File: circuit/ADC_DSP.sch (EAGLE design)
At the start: 57 parts, among them IC1 REG1117, IC3 STM32F40XRXT6, IC4 CS4272, Q1 8MHz, Q2 24.576MHz

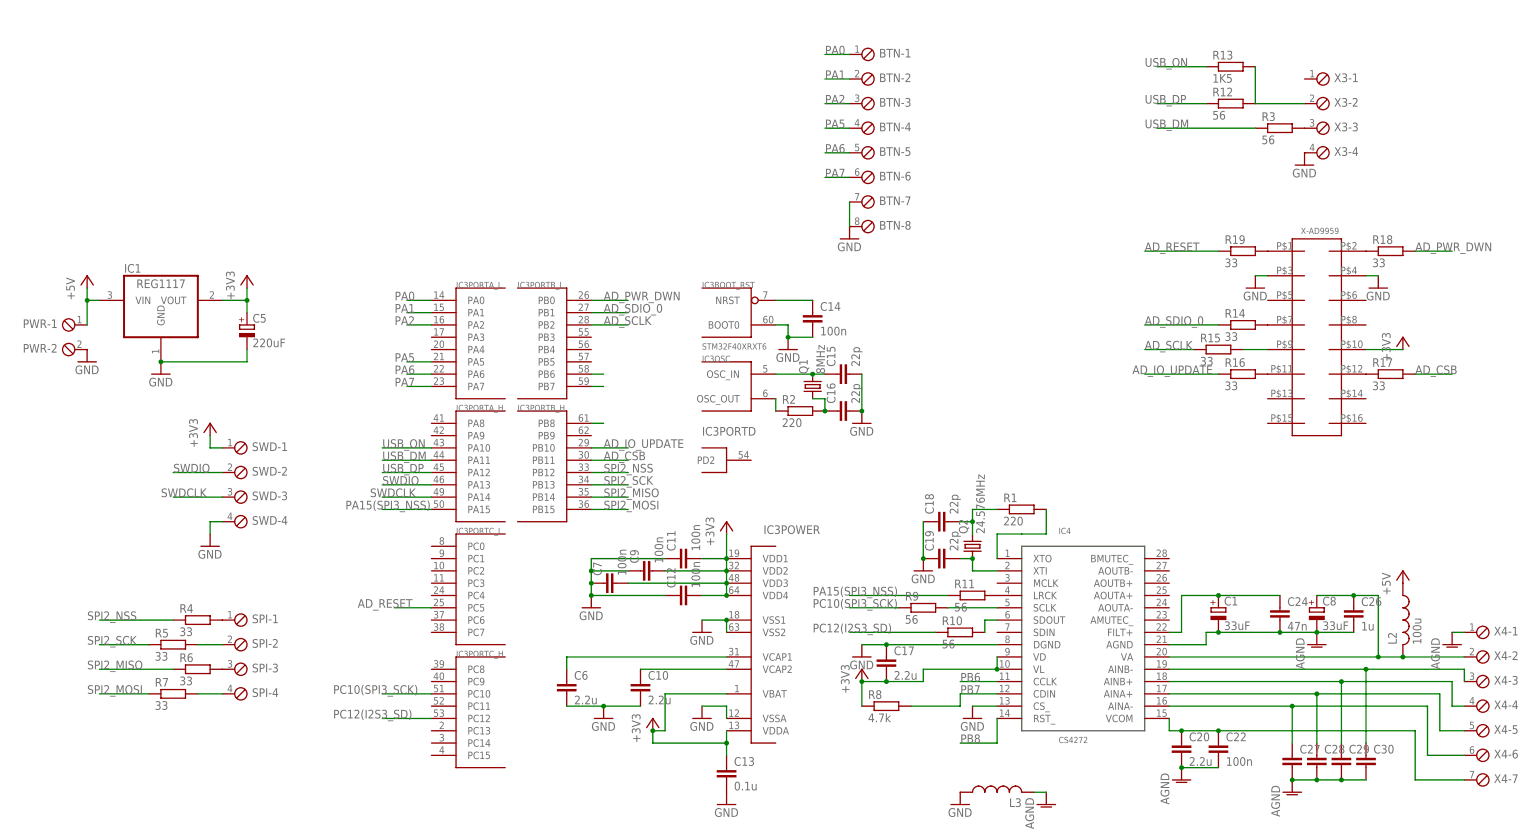
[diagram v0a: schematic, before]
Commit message: - добавили LCD разъем
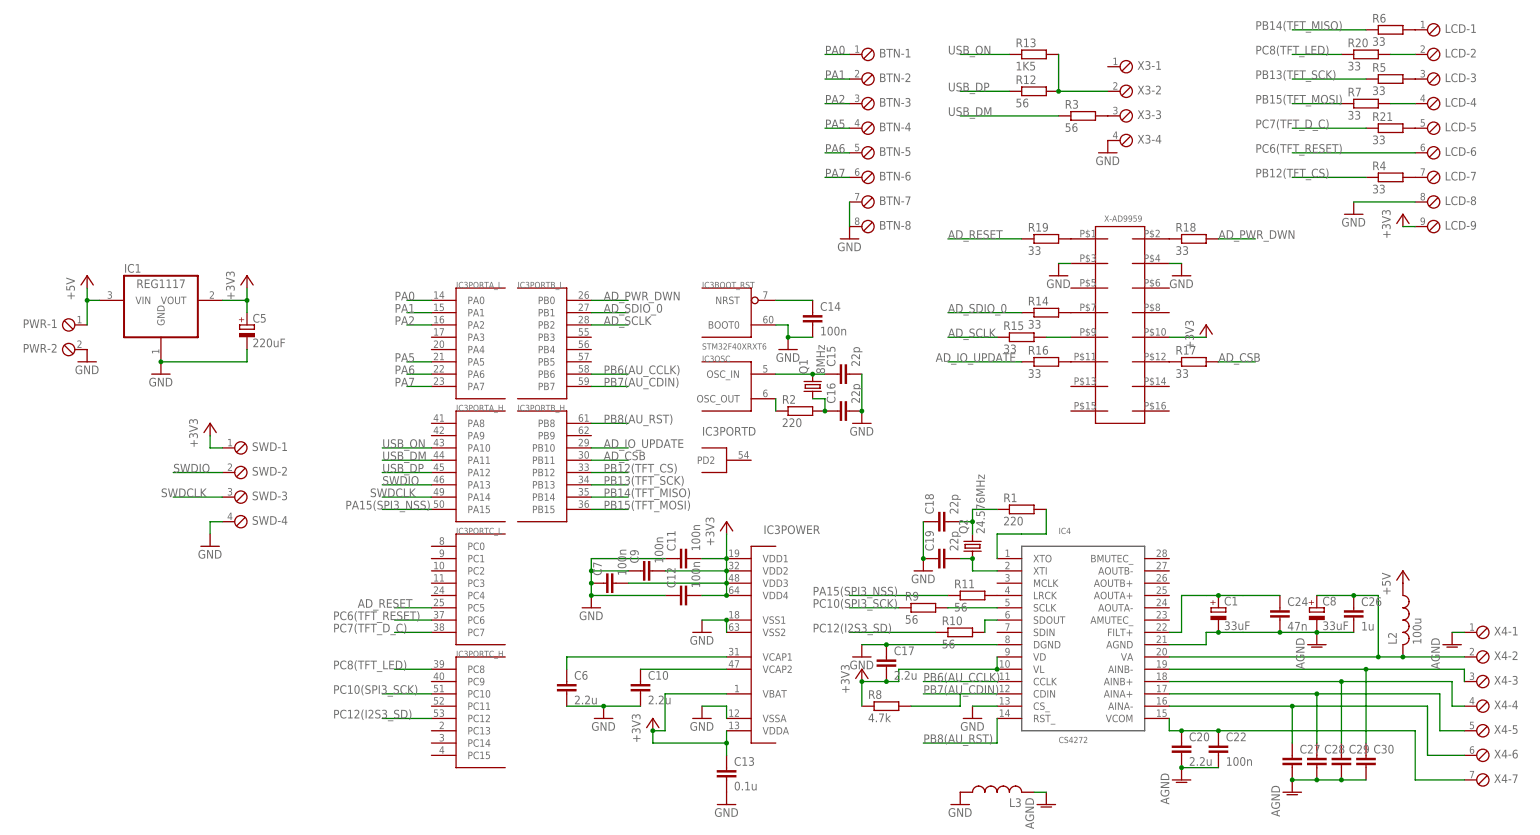
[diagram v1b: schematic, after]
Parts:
- removed SPI: (no value), con-phoenix-254:MPT4
- added LCD: (no value), con-phoenix-254:MPT9
- added R20, R21: 33, rcl:R-EU_R0603
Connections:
- net PB6 renamed PB6(AU_CCLK)
- net PB7 renamed PB7(AU_CDIN)
- net PB8 renamed PB8(AU_RST)
- net SPI2_MISO renamed PB14(TFT_MISO)
- net SPI2_MOSI renamed PB15(TFT_MOSI)
- net SPI2_NSS renamed PB12(TFT_CS)
- net SPI2_SCK renamed PB13(TFT_SCK)
- new net N$34: LCD-7.1, R4.2
- new net N$35: LCD-5.1, R21.2
- new net PC6(TFT_RESET): IC3PORTC_L.PC6, LCD-6.1
- new net PC7(TFT_D_C): IC3PORTC_L.PC7, R21.1
- new net PC8(TFT_LED): IC3PORTC_H.PC8, R20.1
- net +3V3: now also LCD-9.1
- net GND: now also LCD-8.1
- net N$20: now also LCD-1.1, R6.2; no longer R4.2, SPI-1.1
- net N$21: now also LCD-3.1; no longer SPI-2.1
- net N$22: now also LCD-2.1, R20.2; no longer R6.2, SPI-3.1
- net N$24: now also LCD-4.1; no longer SPI-4.1
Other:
- moved on the sheet: R12, R13, R14, R15, R16, R17, R18, R19, R3, R4, R5, R6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

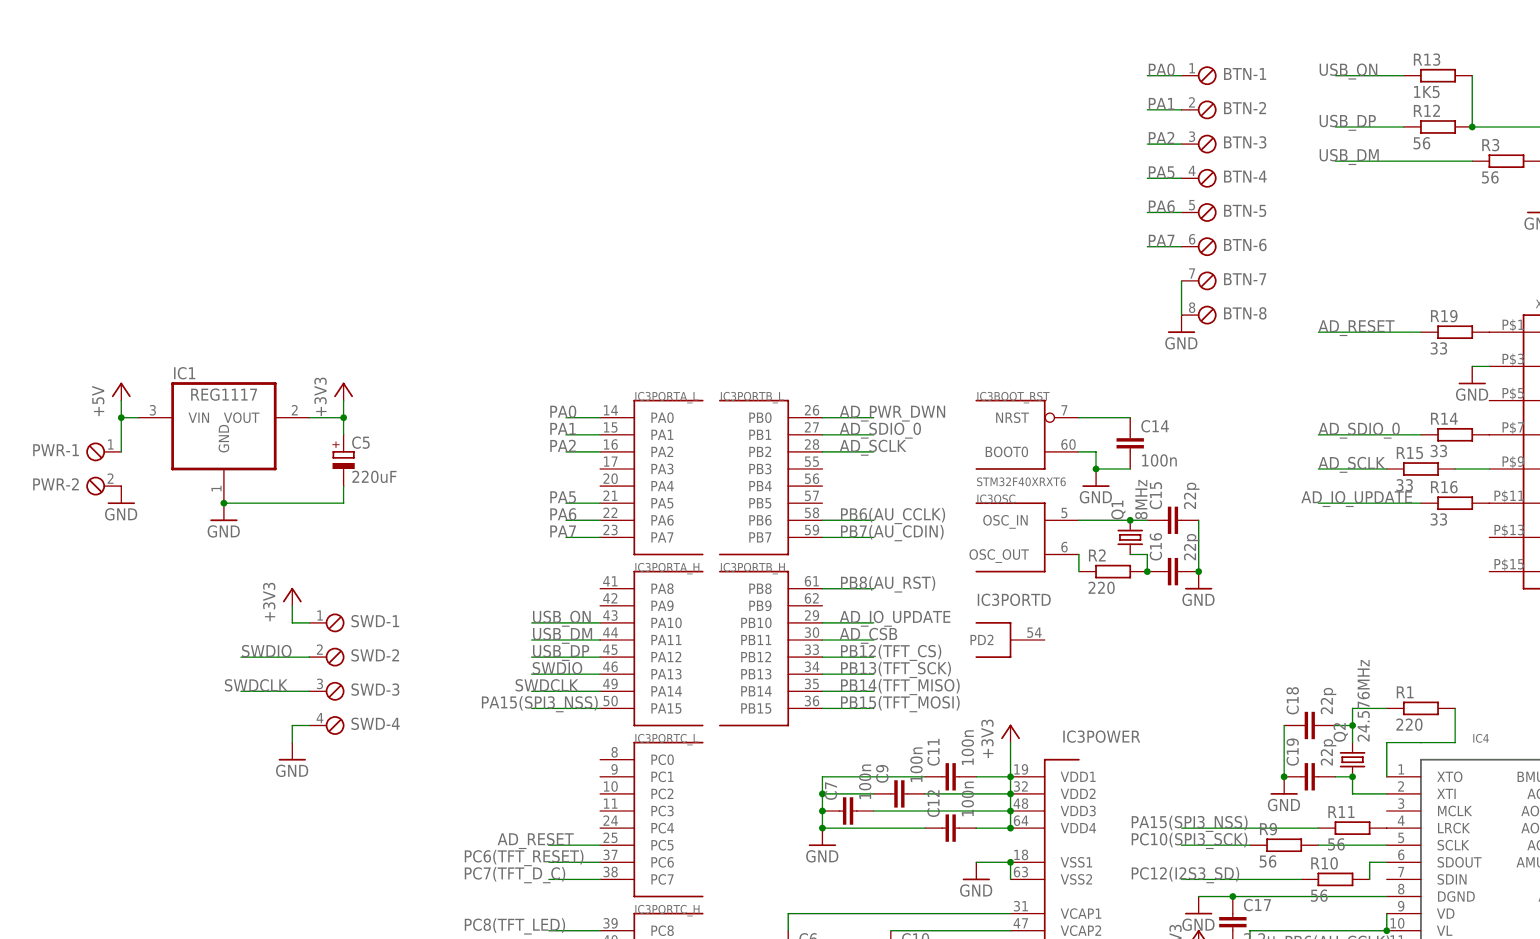
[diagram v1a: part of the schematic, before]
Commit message: - добавил 4 GPIO
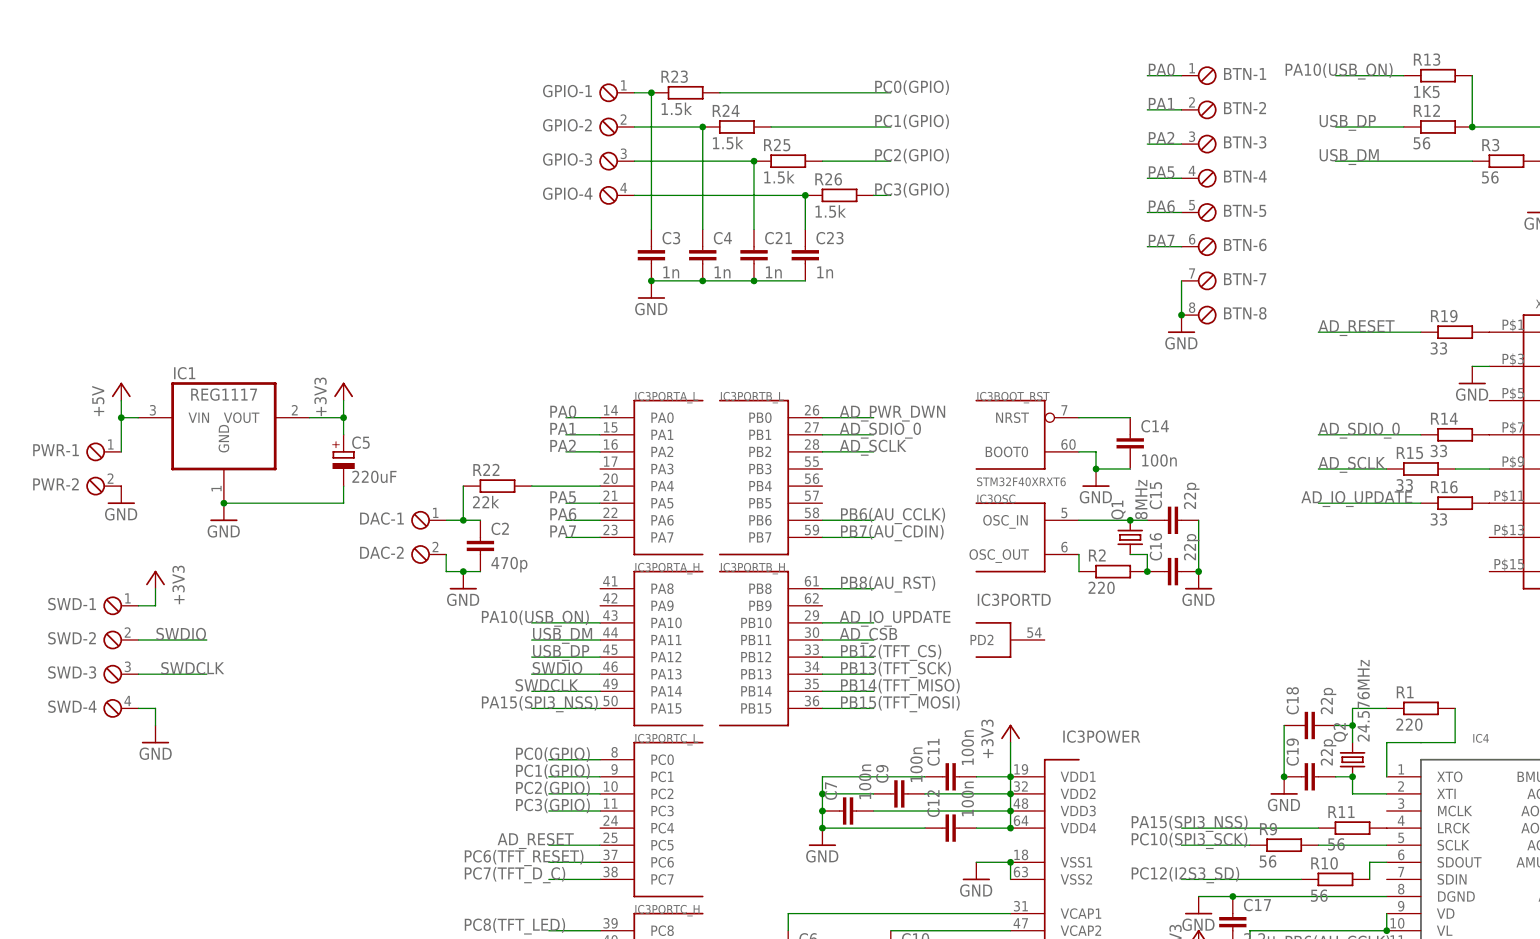
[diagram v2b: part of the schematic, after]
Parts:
- added C2: 470p, rcl:C-EUC0805
- added C21, C23, C3, C4: 1n, rcl:C-EUC0805
- added DAC: (no value), con-phoenix-254:MPT2
- added GPIO: (no value), con-phoenix-254:MPT4
- added R22: 22k, rcl:R-EU_R0603
- added R23, R24, R25, R26: 1.5k, rcl:R-EU_R0603
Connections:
- net USB_ON renamed PA10(USB_ON)
- new net N$36: IC3PORTA_L.PA4, R22.2
- new net N$37: C2.1, DAC-1.1, R22.1
- new net N$38: C3.1, GPIO-1.1, R23.1
- new net N$39: C4.1, GPIO-2.1, R24.1
- new net N$40: C21.1, GPIO-3.1, R25.1
- new net N$41: C23.1, GPIO-4.1, R26.1
- new net PC0(GPIO): IC3PORTC_L.PC0, R23.2
- new net PC1(GPIO): IC3PORTC_L.PC1, R24.2
- new net PC2(GPIO): IC3PORTC_L.PC2, R25.2
- new net PC3(GPIO): IC3PORTC_L.PC3, R26.2
- net GND: now also C2.2, C21.2, C23.2, C3.2, C4.2, DAC-2.1
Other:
- moved on the sheet: SWD-1, SWD-2, SWD-3, SWD-4

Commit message: - развели еще немного
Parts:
- removed C13: 0.1u, rcl:C-EUC0603
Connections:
- net +3V3: no longer C13.1
- net GND: no longer C13.2
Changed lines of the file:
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@@
 <part name="C6" library="rcl" deviceset="C-EU" device="C0603" value="2.2u"/>
 <part name="GND10" library="supply1" deviceset="GND" device=""/>
-<part name="C13" library="rcl" deviceset="C-EU" device="C0603" value="0.1u"/>
 <part name="+3V33" library="supply1" deviceset="+3V3" device=""/>
-<part name="GND13" library="supply1" deviceset="GND" device=""/>
 <part name="GND12" library="supply1" deviceset="GND" device=""/>
 <part name="GND14" library="supply1" deviceset="GND" device=""/>
@@
 <instance part="C6" gate="G$1" x="53.34" y="-2.54"/>
 <instance part="GND10" gate="1" x="60.96" y="-10.16"/>
-<instance part="C13" gate="G$1" x="86.36" y="-20.32"/>
 <instance part="+3V33" gate="G$1" x="71.12" y="-10.16"/>
-<instance part="GND13" gate="1" x="86.36" y="-27.94"/>
 <instance part="GND12" gate="1" x="81.28" y="-10.16"/>
 <instance part="GND14" gate="1" x="99.06" y="66.04"/>
@@
 </segment>
 <segment>
-<pinref part="C13" gate="G$1" pin="2"/>
-<pinref part="GND13" gate="1" pin="GND"/>
-</segment>
-<segment>
 <pinref part="IC3" gate="POWER" pin="VSSA"/>
 <wire x1="86.36" y1="-10.16" x2="86.36" y2="-7.62" width="0.1524" layer="91"/>
@@
 <wire x1="73.66" y1="-12.7" x2="71.12" y2="-12.7" width="0.1524" layer="91"/>
 <junction x="71.12" y="-12.7"/>
-<pinref part="C13" gate="G$1" pin="1"/>
 <pinref part="IC3" gate="POWER" pin="VDDA"/>
 <wire x1="86.36" y1="-15.24" x2="86.36" y2="-12.7" width="0.1524" layer="91"/>
-<wire x1="86.36" y1="-17.78" x2="86.36" y2="-15.24" width="0.1524" layer="91"/>
-<junction x="86.36" y="-15.24"/>
 <wire x1="71.12" y1="-15.24" x2="86.36" y2="-15.24" width="0.1524" layer="91"/>
 </segment>

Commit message: - развели в первом приближении
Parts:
- removed X3: (no value), con-phoenix-254:MPT4
- added USB: (no value), con-phoenix-254:MPT3
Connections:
- net GND: now also USB-3.1; no longer X3-4.1
- net N$16: now also USB-1.1; no longer X3-2.1
- net N$3: now also USB-2.1; no longer X3-3.1
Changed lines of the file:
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@@
 <part name="GND6" library="supply1" deviceset="GND" device=""/>
 <part name="+3V2" library="supply1" deviceset="+3V3" device=""/>
-<part name="X3" library="con-phoenix-254" deviceset="MPT4" device=""/>
 <part name="GND4" library="supply1" deviceset="GND" device=""/>
 <part name="R3" library="rcl" deviceset="R-EU_" device="R0603" value="56"/>
@@
 <part name="R26" library="rcl" deviceset="R-EU_" device="R0603" value="1.5k"/>
 <part name="GND21" library="supply1" deviceset="GND" device=""/>
+<part name="USB" library="con-phoenix-254" deviceset="MPT3" device=""/>
 </parts>
 <sheets>
@@
 <instance part="GND6" gate="1" x="180.34" y="81.28"/>
 <instance part="+3V2" gate="G$1" x="185.42" y="71.12"/>
-<instance part="X3" gate="-1" x="167.64" y="124.46"/>
-<instance part="X3" gate="-2" x="167.64" y="119.38"/>
-<instance part="X3" gate="-3" x="167.64" y="114.3"/>
-<instance part="X3" gate="-4" x="167.64" y="109.22"/>
 <instance part="GND4" gate="1" x="165.1" y="106.68"/>
 <instance part="R3" gate="G$1" x="160.02" y="114.3"/>
@@
 <instance part="R26" gate="G$1" x="60.96" y="109.22"/>
 <instance part="GND21" gate="1" x="33.02" y="93.98"/>
+<instance part="USB" gate="-1" x="167.64" y="119.38"/>
+<instance part="USB" gate="-2" x="167.64" y="114.3"/>
+<instance part="USB" gate="-3" x="167.64" y="109.22"/>
 </instances>
 <busses>
@@
 </segment>
 <segment>
-<pinref part="X3" gate="-4" pin="1"/>
-<pinref part="GND4" gate="1" pin="GND"/>
-</segment>
-<segment>
 <pinref part="PWR" gate="-2" pin="1"/>
 <pinref part="GND7" gate="1" pin="GND"/>
@@
 <junction x="40.64" y="96.52"/>
 <junction x="48.26" y="96.52"/>
+</segment>
+<segment>
+<pinref part="GND4" gate="1" pin="GND"/>
+<pinref part="USB" gate="-3" pin="1"/>
 </segment>
 </net>
@@
 </segment>
 </net>
-<net name="N$3" class="0">
-<segment>
-<pinref part="X3" gate="-3" pin="1"/>
-<pinref part="R3" gate="G$1" pin="2"/>
-</segment>
-</net>
 <net name="N$16" class="0">
 <segment>
-<pinref part="X3" gate="-2" pin="1"/>
 <pinref part="R12" gate="G$1" pin="2"/>
 <wire x1="165.1" y1="119.38" x2="154.94" y2="119.38" width="0.1524" layer="91"/>
@@
 <wire x1="154.94" y1="127" x2="154.94" y2="119.38" width="0.1524" layer="91"/>
 <junction x="154.94" y="119.38"/>
+<pinref part="USB" gate="-1" pin="1"/>
 </segment>
 </net>
@@
 </segment>
 </net>
+<net name="N$3" class="0">
+<segment>
+<pinref part="R3" gate="G$1" pin="2"/>
+<pinref part="USB" gate="-2" pin="1"/>
+</segment>
+</net>
